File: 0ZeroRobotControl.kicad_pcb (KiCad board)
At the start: 4 copper layers, 100 x 100 mm, 249 parts, among them IC1 TC4427A, IC10 L6470, IC2 TC4427A, IC3 TC4427A, IC4 CY25811, IC5 L6470, IC6 L6470, IC7 L6470, IC8 L6470, IC9 L6470, J1 CONN_02X08, J2 CONN_02X03, J3 USB Micro-B Power Out, P1 RaspPi 40pin Conn, P10 5452027, P11 Thermistor_Inputs, P12 MOTOR-1, P13 MOTOR-2, P14 MOTOR-3, P15 MOTOR-4, P16 MOTOR-5, P17 MOTOR-6, P18 SW1, P19 SW2, P2 XT60PW-M, P20 SW3, P21 SW4, P22 SW5, P23 SW6, P25 CONN_01X01, P26 CONN_01X01, P3 XT60PW-M, P4 XT60PW-M, P5 XT30PW-F, P6 XT30PW-F, P7 XT30PW-F, P8 5452027, P9 5452027, Q1 AOT240L, Q2 AOT240L, Q3 AOT240L, Q4 AOT2618L, Q5 AOT2618L, Q6 AOT2618L, U1 LM78L12ACZ, U2 LM78L12ACZ, U3 LM78L12ACZ, U4 MCP3204, U7 R-78E3.3-1.0, U8 R-78E5.0-1.0, Y1 Crystal 32MHz

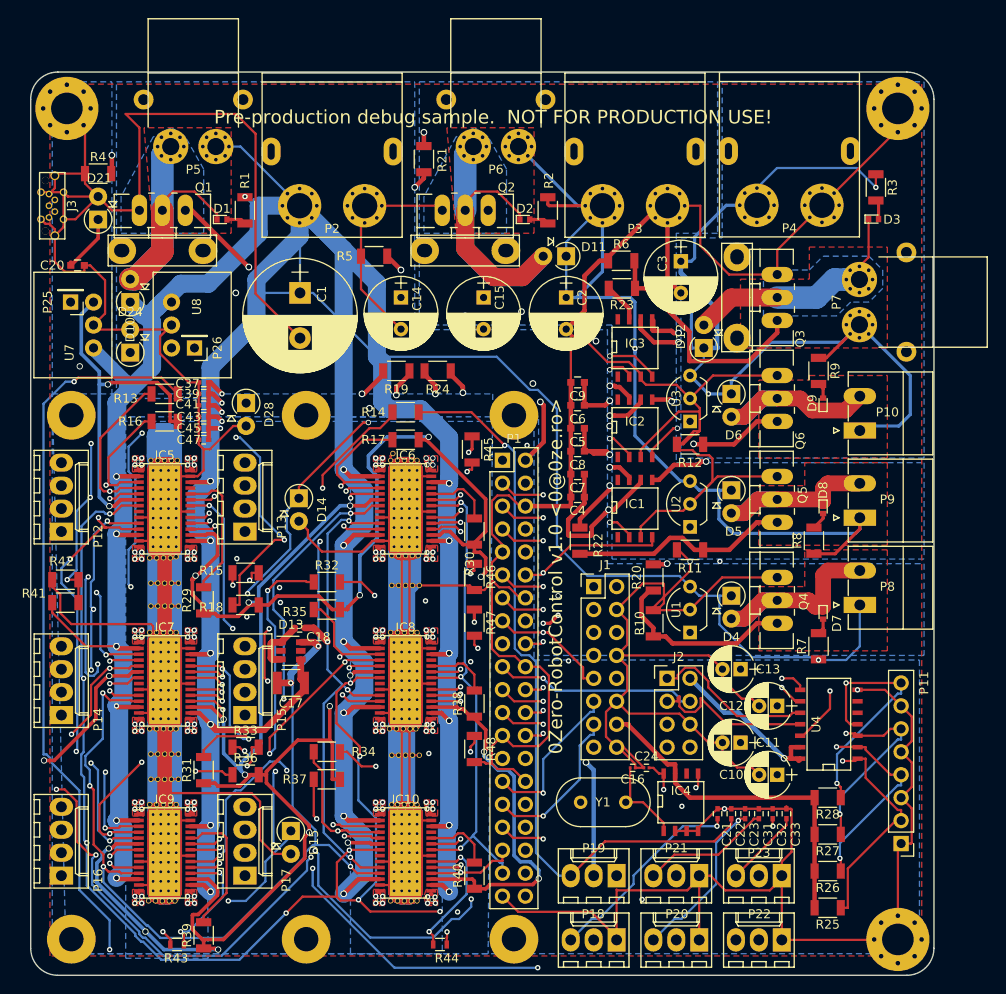
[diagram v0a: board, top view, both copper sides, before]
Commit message: added more vias for heat dispersion of stepper controllers, also fixed some tracks/vias.
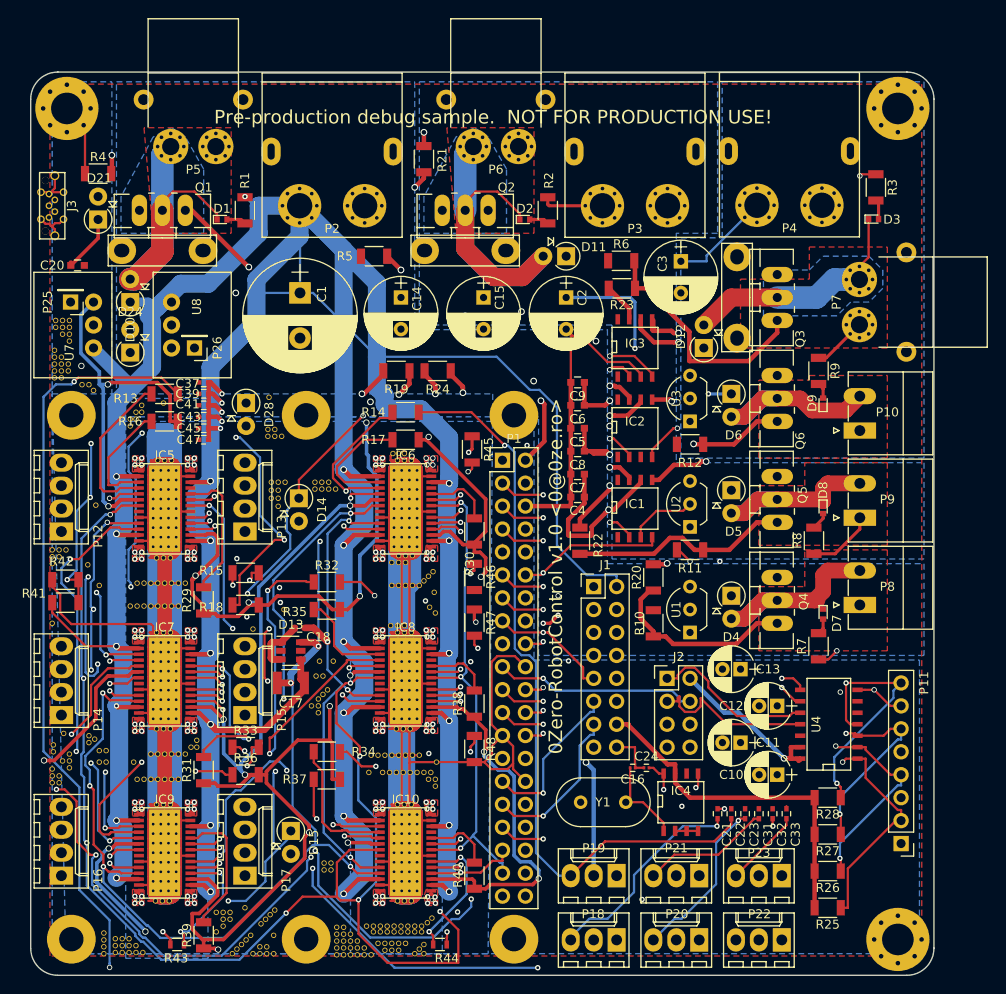
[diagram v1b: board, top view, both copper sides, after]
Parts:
- removed REF1, REF10, REF21, REF25, REF26, REF30, REF36, REF40, REF45, REF6, REF60, REF65, REF76, REF80, REF81, REF85, REF86, REF90: Via__0.6-0.4, PiPrinter:Via__0.6-0.4
- removed the REF5 at (35.3, 63.2)
- removed the REF56 at (61.8, 82.3)
- removed the REF61 at (61.7, 93.0)
- removed the REF66 at (64.8, 101.3)
- removed the REF66 at (62.0, 101.3)
- added REF42: Via__0.6-0.4, PiPrinter:Via__0.6-0.4, F.Cu at (63.5, 74.5)
- added REF42: Via__0.6-0.4, PiPrinter:Via__0.6-0.4, F.Cu at (62.7, 74.5)
- added REF5: Via__0.6-0.4, PiPrinter:Via__0.6-0.4, F.Cu at (26.3, 47.8)
- added REF5: Via__0.6-0.4, PiPrinter:Via__0.6-0.4, F.Cu at (26.2, 52.6)
- added REF5: Via__0.6-0.4, PiPrinter:Via__0.6-0.4, F.Cu at (26.2, 53.3)
- added REF5: Via__0.6-0.4, PiPrinter:Via__0.6-0.4, F.Cu at (25.4, 51.8)
- added REF5: Via__0.6-0.4, PiPrinter:Via__0.6-0.4, F.Cu at (25.4, 52.6)
- added REF5: Via__0.6-0.4, PiPrinter:Via__0.6-0.4, F.Cu at (25.4, 53.3)
- added REF5: Via__0.6-0.4, PiPrinter:Via__0.6-0.4, F.Cu at (25.4, 54.1)
- added REF5: Via__0.6-0.4, PiPrinter:Via__0.6-0.4, F.Cu at (24.6, 51.1)
- added REF5: Via__0.6-0.4, PiPrinter:Via__0.6-0.4, F.Cu at (24.6, 51.8)
- added REF5: Via__0.6-0.4, PiPrinter:Via__0.6-0.4, F.Cu at (24.6, 52.6)
- added REF5: Via__0.6-0.4, PiPrinter:Via__0.6-0.4, F.Cu at (24.6, 53.3)
- added REF5: Via__0.6-0.4, PiPrinter:Via__0.6-0.4, F.Cu at (26.3, 48.5)
- added REF5: Via__0.6-0.4, PiPrinter:Via__0.6-0.4, F.Cu at (24.6, 54.1)
- added REF5: Via__0.6-0.4, PiPrinter:Via__0.6-0.4, F.Cu at (29.0, 55.5)
- added REF5: Via__0.6-0.4, PiPrinter:Via__0.6-0.4, F.Cu at (28.4, 54.9)
- added REF5: Via__0.6-0.4, PiPrinter:Via__0.6-0.4, F.Cu at (27.7, 54.9)
- added REF5: Via__0.6-0.4, PiPrinter:Via__0.6-0.4, F.Cu at (36.7, 56.9)
- added REF5: Via__0.6-0.4, PiPrinter:Via__0.6-0.4, F.Cu at (33.0, 59.4)
- added REF5: Via__0.6-0.4, PiPrinter:Via__0.6-0.4, F.Cu at (33.0, 58.7)
- added REF5: Via__0.6-0.4, PiPrinter:Via__0.6-0.4, F.Cu at (33.7, 58.7)
- added REF5: Via__0.6-0.4, PiPrinter:Via__0.6-0.4, F.Cu at (33.7, 57.9)
- added REF5: Via__0.6-0.4, PiPrinter:Via__0.6-0.4, F.Cu at (34.3, 57.9)
- added REF5: Via__0.6-0.4, PiPrinter:Via__0.6-0.4, F.Cu at (26.3, 50.0)
- added REF5: Via__0.6-0.4, PiPrinter:Via__0.6-0.4, F.Cu at (34.3, 57.1)
- added REF5: Via__0.6-0.4, PiPrinter:Via__0.6-0.4, F.Cu at (26.3, 49.3)
- added REF5: Via__0.6-0.4, PiPrinter:Via__0.6-0.4, F.Cu at (25.5, 49.3)
- added REF5: Via__0.6-0.4, PiPrinter:Via__0.6-0.4, F.Cu at (25.5, 48.5)
- added REF5: Via__0.6-0.4, PiPrinter:Via__0.6-0.4, F.Cu at (25.5, 47.8)
- added REF5: Via__0.6-0.4, PiPrinter:Via__0.6-0.4, F.Cu at (24.8, 48.5)
- added REF5: Via__0.6-0.4, PiPrinter:Via__0.6-0.4, F.Cu at (24.8, 47.8)
- added REF50: Via__0.6-0.4, PiPrinter:Via__0.6-0.4, F.Cu at (66.8, 80.1)
- added REF50: Via__0.6-0.4, PiPrinter:Via__0.6-0.4, F.Cu at (66.2, 79.5)
- added REF50: Via__0.6-0.4, PiPrinter:Via__0.6-0.4, F.Cu at (66.5, 75.6)
- added REF50: Via__0.6-0.4, PiPrinter:Via__0.6-0.4, F.Cu at (66.0, 76.1)
- added REF50: Via__0.6-0.4, PiPrinter:Via__0.6-0.4, F.Cu at (65.5, 76.6)
- added REF56: Via__0.6-0.4, PiPrinter:Via__0.6-0.4, F.Cu at (66.7, 77.9)
- added REF56: Via__0.6-0.4, PiPrinter:Via__0.6-0.4, F.Cu at (63.4, 81.5)
- added REF56: Via__0.6-0.4, PiPrinter:Via__0.6-0.4, F.Cu at (62.6, 81.5)
- added REF56: Via__0.6-0.4, PiPrinter:Via__0.6-0.4, F.Cu at (61.8, 81.5)
- added REF61: Via__0.6-0.4, PiPrinter:Via__0.6-0.4, F.Cu at (48.4, 56.3)
- added REF61: Via__0.6-0.4, PiPrinter:Via__0.6-0.4, F.Cu at (49.4, 66.5)
- added REF61: Via__0.6-0.4, PiPrinter:Via__0.6-0.4, F.Cu at (48.6, 66.5)
- added REF61: Via__0.6-0.4, PiPrinter:Via__0.6-0.4, F.Cu at (50.2, 65.7)
- added REF61: Via__0.6-0.4, PiPrinter:Via__0.6-0.4, F.Cu at (49.4, 65.7)
- added REF61: Via__0.6-0.4, PiPrinter:Via__0.6-0.4, F.Cu at (48.6, 65.7)
- added REF61: Via__0.6-0.4, PiPrinter:Via__0.6-0.4, F.Cu at (55.8, 66.4)
- added REF61: Via__0.6-0.4, PiPrinter:Via__0.6-0.4, F.Cu at (55.0, 66.4)
- added REF61: Via__0.6-0.4, PiPrinter:Via__0.6-0.4, F.Cu at (54.2, 66.4)
- added REF61: Via__0.6-0.4, PiPrinter:Via__0.6-0.4, F.Cu at (53.5, 66.4)
- added REF61: Via__0.6-0.4, PiPrinter:Via__0.6-0.4, F.Cu at (55.0, 65.7)
- added REF61: Via__0.6-0.4, PiPrinter:Via__0.6-0.4, F.Cu at (49.8, 60.6)
- added REF61: Via__0.6-0.4, PiPrinter:Via__0.6-0.4, F.Cu at (54.2, 65.7)
- added REF61: Via__0.6-0.4, PiPrinter:Via__0.6-0.4, F.Cu at (53.5, 65.7)
- added REF61: Via__0.6-0.4, PiPrinter:Via__0.6-0.4, F.Cu at (46.6, 81.9)
- added REF61: Via__0.6-0.4, PiPrinter:Via__0.6-0.4, F.Cu at (50.0, 79.8)
- added REF61: Via__0.6-0.4, PiPrinter:Via__0.6-0.4, F.Cu at (55.5, 85.5)
- added REF61: Via__0.6-0.4, PiPrinter:Via__0.6-0.4, F.Cu at (54.0, 85.5)
- added REF61: Via__0.6-0.4, PiPrinter:Via__0.6-0.4, F.Cu at (54.4, 87.1)
- added REF61: Via__0.6-0.4, PiPrinter:Via__0.6-0.4, F.Cu at (53.6, 87.1)
- added REF61: Via__0.6-0.4, PiPrinter:Via__0.6-0.4, F.Cu at (53.1, 90.4)
- added REF61: Via__0.6-0.4, PiPrinter:Via__0.6-0.4, F.Cu at (53.8, 91.2)
- added REF61: Via__0.6-0.4, PiPrinter:Via__0.6-0.4, F.Cu at (49.0, 60.6)
- added REF61: Via__0.6-0.4, PiPrinter:Via__0.6-0.4, F.Cu at (53.8, 90.4)
- added REF61: Via__0.6-0.4, PiPrinter:Via__0.6-0.4, F.Cu at (53.8, 89.7)
- added REF61: Via__0.6-0.4, PiPrinter:Via__0.6-0.4, F.Cu at (54.4, 89.2)
- added REF61: Via__0.6-0.4, PiPrinter:Via__0.6-0.4, F.Cu at (54.9, 88.6)
- added REF61: Via__0.6-0.4, PiPrinter:Via__0.6-0.4, F.Cu at (48.3, 60.6)
- added REF61: Via__0.6-0.4, PiPrinter:Via__0.6-0.4, F.Cu at (49.0, 59.8)
- added REF61: Via__0.6-0.4, PiPrinter:Via__0.6-0.4, F.Cu at (48.3, 59.8)
- added REF61: Via__0.6-0.4, PiPrinter:Via__0.6-0.4, F.Cu at (49.4, 68.3)
- added REF61: Via__0.6-0.4, PiPrinter:Via__0.6-0.4, F.Cu at (49.4, 67.4)
- added REF61: Via__0.6-0.4, PiPrinter:Via__0.6-0.4, F.Cu at (48.6, 67.4)
- added REF70: Via__0.6-0.4, PiPrinter:Via__0.6-0.4, F.Cu at (25.1, 98.2)
- added REF70: Via__0.6-0.4, PiPrinter:Via__0.6-0.4, F.Cu at (25.1, 73.2)
- added REF70: Via__0.6-0.4, PiPrinter:Via__0.6-0.4, F.Cu at (55.9, 117.2)
- added REF70: Via__0.6-0.4, PiPrinter:Via__0.6-0.4, F.Cu at (58.2, 116.5)
- added REF70: Via__0.6-0.4, PiPrinter:Via__0.6-0.4, F.Cu at (57.4, 116.5)
- added REF70: Via__0.6-0.4, PiPrinter:Via__0.6-0.4, F.Cu at (56.6, 116.5)
- added REF70: Via__0.6-0.4, PiPrinter:Via__0.6-0.4, F.Cu at (55.9, 116.5)
- added REF70: Via__0.6-0.4, PiPrinter:Via__0.6-0.4, F.Cu at (57.4, 115.7)
- added REF70: Via__0.6-0.4, PiPrinter:Via__0.6-0.4, F.Cu at (56.6, 115.7)
- added REF70: Via__0.6-0.4, PiPrinter:Via__0.6-0.4, F.Cu at (55.9, 115.7)
- added REF70: Via__0.6-0.4, PiPrinter:Via__0.6-0.4, F.Cu at (56.6, 114.9)
- added REF70: Via__0.6-0.4, PiPrinter:Via__0.6-0.4, F.Cu at (55.9, 114.9)
- added REF70: Via__0.6-0.4, PiPrinter:Via__0.6-0.4, F.Cu at (24.4, 74.7)
- added REF70: Via__0.6-0.4, PiPrinter:Via__0.6-0.4, F.Cu at (65.5, 117.9)
- added REF70: Via__0.6-0.4, PiPrinter:Via__0.6-0.4, F.Cu at (64.5, 117.9)
- added REF70: Via__0.6-0.4, PiPrinter:Via__0.6-0.4, F.Cu at (65.0, 117.3)
- added REF70: Via__0.6-0.4, PiPrinter:Via__0.6-0.4, F.Cu at (65.5, 116.8)
- added REF70: Via__0.6-0.4, PiPrinter:Via__0.6-0.4, F.Cu at (62.7, 117.5)
- added REF70: Via__0.6-0.4, PiPrinter:Via__0.6-0.4, F.Cu at (62.0, 117.5)
- added REF70: Via__0.6-0.4, PiPrinter:Via__0.6-0.4, F.Cu at (61.2, 117.5)
- added REF70: Via__0.6-0.4, PiPrinter:Via__0.6-0.4, F.Cu at (63.5, 116.7)
- added REF70: Via__0.6-0.4, PiPrinter:Via__0.6-0.4, F.Cu at (62.7, 116.7)
- added REF70: Via__0.6-0.4, PiPrinter:Via__0.6-0.4, F.Cu at (62.0, 116.7)
- added REF70: Via__0.6-0.4, PiPrinter:Via__0.6-0.4, F.Cu at (24.4, 73.9)
- added REF70: Via__0.6-0.4, PiPrinter:Via__0.6-0.4, F.Cu at (61.2, 116.7)
- added REF70: Via__0.6-0.4, PiPrinter:Via__0.6-0.4, F.Cu at (60.5, 116.7)
- added REF70: Via__0.6-0.4, PiPrinter:Via__0.6-0.4, F.Cu at (65.3, 115.4)
- added REF70: Via__0.6-0.4, PiPrinter:Via__0.6-0.4, F.Cu at (64.5, 115.4)
- added REF70: Via__0.6-0.4, PiPrinter:Via__0.6-0.4, F.Cu at (63.8, 115.4)
- added REF70: Via__0.6-0.4, PiPrinter:Via__0.6-0.4, F.Cu at (63.0, 115.4)
- added REF70: Via__0.6-0.4, PiPrinter:Via__0.6-0.4, F.Cu at (62.2, 115.4)
- added REF70: Via__0.6-0.4, PiPrinter:Via__0.6-0.4, F.Cu at (61.5, 115.4)
- added REF70: Via__0.6-0.4, PiPrinter:Via__0.6-0.4, F.Cu at (60.7, 115.4)
- added REF70: Via__0.6-0.4, PiPrinter:Via__0.6-0.4, F.Cu at (59.9, 115.4)
- added REF70: Via__0.6-0.4, PiPrinter:Via__0.6-0.4, F.Cu at (24.4, 73.2)
- added REF70: Via__0.6-0.4, PiPrinter:Via__0.6-0.4, F.Cu at (66.4, 113.9)
- added REF70: Via__0.6-0.4, PiPrinter:Via__0.6-0.4, F.Cu at (65.9, 114.4)
- added REF70: Via__0.6-0.4, PiPrinter:Via__0.6-0.4, F.Cu at (65.3, 114.8)
- added REF70: Via__0.6-0.4, PiPrinter:Via__0.6-0.4, F.Cu at (64.5, 114.8)
- added REF70: Via__0.6-0.4, PiPrinter:Via__0.6-0.4, F.Cu at (63.8, 114.8)
- added REF70: Via__0.6-0.4, PiPrinter:Via__0.6-0.4, F.Cu at (63.0, 114.8)
- added REF70: Via__0.6-0.4, PiPrinter:Via__0.6-0.4, F.Cu at (62.2, 114.8)
- added REF70: Via__0.6-0.4, PiPrinter:Via__0.6-0.4, F.Cu at (61.5, 114.8)
- added REF70: Via__0.6-0.4, PiPrinter:Via__0.6-0.4, F.Cu at (60.7, 114.8)
- added REF70: Via__0.6-0.4, PiPrinter:Via__0.6-0.4, F.Cu at (59.9, 114.8)
- added REF70: Via__0.6-0.4, PiPrinter:Via__0.6-0.4, F.Cu at (24.4, 81.3)
- added REF70: Via__0.6-0.4, PiPrinter:Via__0.6-0.4, F.Cu at (59.2, 114.8)
- added REF70: Via__0.6-0.4, PiPrinter:Via__0.6-0.4, F.Cu at (66.9, 96.6)
- added REF70: Via__0.6-0.4, PiPrinter:Via__0.6-0.4, F.Cu at (61.0, 97.8)
- added REF70: Via__0.6-0.4, PiPrinter:Via__0.6-0.4, F.Cu at (61.7, 97.8)
- added REF70: Via__0.6-0.4, PiPrinter:Via__0.6-0.4, F.Cu at (62.5, 97.8)
- added REF70: Via__0.6-0.4, PiPrinter:Via__0.6-0.4, F.Cu at (59.7, 95.9)
- added REF70: Via__0.6-0.4, PiPrinter:Via__0.6-0.4, F.Cu at (60.5, 95.9)
- added REF70: Via__0.6-0.4, PiPrinter:Via__0.6-0.4, F.Cu at (61.2, 95.9)
- added REF70: Via__0.6-0.4, PiPrinter:Via__0.6-0.4, F.Cu at (66.8, 99.3)
- added REF70: Via__0.6-0.4, PiPrinter:Via__0.6-0.4, F.Cu at (66.8, 98.6)
- added REF70: Via__0.6-0.4, PiPrinter:Via__0.6-0.4, F.Cu at (28.3, 74.8)
- added REF70: Via__0.6-0.4, PiPrinter:Via__0.6-0.4, F.Cu at (66.0, 98.6)
- added REF70: Via__0.6-0.4, PiPrinter:Via__0.6-0.4, F.Cu at (66.3, 97.8)
- added REF70: Via__0.6-0.4, PiPrinter:Via__0.6-0.4, F.Cu at (65.5, 97.8)
- added REF70: Via__0.6-0.4, PiPrinter:Via__0.6-0.4, F.Cu at (64.8, 97.8)
- added REF70: Via__0.6-0.4, PiPrinter:Via__0.6-0.4, F.Cu at (29.6, 77.1)
- added REF70: Via__0.6-0.4, PiPrinter:Via__0.6-0.4, F.Cu at (39.1, 76.8)
- added REF70: Via__0.6-0.4, PiPrinter:Via__0.6-0.4, F.Cu at (33.8, 76.8)
- added REF70: Via__0.6-0.4, PiPrinter:Via__0.6-0.4, F.Cu at (34.5, 76.8)
- added REF70: Via__0.6-0.4, PiPrinter:Via__0.6-0.4, F.Cu at (30.1, 117.9)
- added REF70: Via__0.6-0.4, PiPrinter:Via__0.6-0.4, F.Cu at (33.0, 79.4)
- added REF70: Via__0.6-0.4, PiPrinter:Via__0.6-0.4, F.Cu at (33.8, 79.4)
- added REF70: Via__0.6-0.4, PiPrinter:Via__0.6-0.4, F.Cu at (34.5, 79.4)
- added REF70: Via__0.6-0.4, PiPrinter:Via__0.6-0.4, F.Cu at (24.4, 98.9)
- added REF70: Via__0.6-0.4, PiPrinter:Via__0.6-0.4, F.Cu at (24.4, 98.2)
- added REF70: Via__0.6-0.4, PiPrinter:Via__0.6-0.4, F.Cu at (24.4, 97.4)
- added REF70: Via__0.6-0.4, PiPrinter:Via__0.6-0.4, F.Cu at (25.1, 98.9)
- added REF70: Via__0.6-0.4, PiPrinter:Via__0.6-0.4, F.Cu at (25.7, 93.5)
- added REF70: Via__0.6-0.4, PiPrinter:Via__0.6-0.4, F.Cu at (24.5, 94.7)
- added REF70: Via__0.6-0.4, PiPrinter:Via__0.6-0.4, F.Cu at (24.5, 95.5)
- added REF70: Via__0.6-0.4, PiPrinter:Via__0.6-0.4, F.Cu at (31.4, 117.7)
- added REF70: Via__0.6-0.4, PiPrinter:Via__0.6-0.4, F.Cu at (26.3, 97.3)
- added REF70: Via__0.6-0.4, PiPrinter:Via__0.6-0.4, F.Cu at (26.3, 95.8)
- added REF70: Via__0.6-0.4, PiPrinter:Via__0.6-0.4, F.Cu at (26.3, 96.5)
- added REF70: Via__0.6-0.4, PiPrinter:Via__0.6-0.4, F.Cu at (25.5, 96.5)
- added REF70: Via__0.6-0.4, PiPrinter:Via__0.6-0.4, F.Cu at (29.1, 94.1)
- added REF70: Via__0.6-0.4, PiPrinter:Via__0.6-0.4, F.Cu at (28.4, 94.5)
- added REF70: Via__0.6-0.4, PiPrinter:Via__0.6-0.4, F.Cu at (28.4, 93.7)
- added REF70: Via__0.6-0.4, PiPrinter:Via__0.6-0.4, F.Cu at (29.6, 95.4)
- added REF70: Via__0.6-0.4, PiPrinter:Via__0.6-0.4, F.Cu at (30.4, 95.4)
- added REF70: Via__0.6-0.4, PiPrinter:Via__0.6-0.4, F.Cu at (29.6, 96.6)
- added REF70: Via__0.6-0.4, PiPrinter:Via__0.6-0.4, F.Cu at (59.4, 97.8)
- added REF70: Via__0.6-0.4, PiPrinter:Via__0.6-0.4, F.Cu at (30.4, 96.6)
- added REF70: Via__0.6-0.4, PiPrinter:Via__0.6-0.4, F.Cu at (40.4, 94.2)
- added REF70: Via__0.6-0.4, PiPrinter:Via__0.6-0.4, F.Cu at (40.4, 95.0)
- added REF70: Via__0.6-0.4, PiPrinter:Via__0.6-0.4, F.Cu at (39.8, 95.0)
- added REF70: Via__0.6-0.4, PiPrinter:Via__0.6-0.4, F.Cu at (39.1, 95.8)
- added REF70: Via__0.6-0.4, PiPrinter:Via__0.6-0.4, F.Cu at (33.4, 96.6)
- added REF70: Via__0.6-0.4, PiPrinter:Via__0.6-0.4, F.Cu at (33.8, 98.6)
- added REF70: Via__0.6-0.4, PiPrinter:Via__0.6-0.4, F.Cu at (34.5, 98.6)
- added REF70: Via__0.6-0.4, PiPrinter:Via__0.6-0.4, F.Cu at (42.5, 115.4)
- added REF70: Via__0.6-0.4, PiPrinter:Via__0.6-0.4, F.Cu at (43.3, 114.8)
- added REF70: Via__0.6-0.4, PiPrinter:Via__0.6-0.4, F.Cu at (64.0, 97.8)
- added REF70: Via__0.6-0.4, PiPrinter:Via__0.6-0.4, F.Cu at (44.1, 114.0)
- added REF70: Via__0.6-0.4, PiPrinter:Via__0.6-0.4, F.Cu at (43.3, 114.0)
- added REF70: Via__0.6-0.4, PiPrinter:Via__0.6-0.4, F.Cu at (44.1, 113.3)
- added REF70: Via__0.6-0.4, PiPrinter:Via__0.6-0.4, F.Cu at (42.5, 113.3)
- added REF70: Via__0.6-0.4, PiPrinter:Via__0.6-0.4, F.Cu at (43.3, 113.3)
- added REF70: Via__0.6-0.4, PiPrinter:Via__0.6-0.4, F.Cu at (45.7, 112.8)
- added REF70: Via__0.6-0.4, PiPrinter:Via__0.6-0.4, F.Cu at (49.0, 113.0)
- added REF70: Via__0.6-0.4, PiPrinter:Via__0.6-0.4, F.Cu at (48.5, 113.5)
- added REF70: Via__0.6-0.4, PiPrinter:Via__0.6-0.4, F.Cu at (48.0, 114.0)
- added REF70: Via__0.6-0.4, PiPrinter:Via__0.6-0.4, F.Cu at (47.5, 114.6)
- added REF70: Via__0.6-0.4, PiPrinter:Via__0.6-0.4, F.Cu at (63.2, 97.8)
- added REF70: Via__0.6-0.4, PiPrinter:Via__0.6-0.4, F.Cu at (46.4, 115.8)
- added REF70: Via__0.6-0.4, PiPrinter:Via__0.6-0.4, F.Cu at (45.8, 116.3)
- added REF70: Via__0.6-0.4, PiPrinter:Via__0.6-0.4, F.Cu at (45.3, 116.8)
- added REF70: Via__0.6-0.4, PiPrinter:Via__0.6-0.4, F.Cu at (44.8, 117.3)
- added REF70: Via__0.6-0.4, PiPrinter:Via__0.6-0.4, F.Cu at (44.3, 117.9)
- added REF70: Via__0.6-0.4, PiPrinter:Via__0.6-0.4, F.Cu at (30.1, 117.1)
- added REF70: Via__0.6-0.4, PiPrinter:Via__0.6-0.4, F.Cu at (30.1, 115.6)
- added REF70: Via__0.6-0.4, PiPrinter:Via__0.6-0.4, F.Cu at (30.1, 116.3)
- added REF70: Via__0.6-0.4, PiPrinter:Via__0.6-0.4, F.Cu at (34.4, 117.7)
- added REF70: Via__0.6-0.4, PiPrinter:Via__0.6-0.4, F.Cu at (33.7, 117.7)
- added REF70: Via__0.6-0.4, PiPrinter:Via__0.6-0.4, F.Cu at (29.2, 68.2)
- added REF70: Via__0.6-0.4, PiPrinter:Via__0.6-0.4, F.Cu at (32.9, 117.7)
- added REF70: Via__0.6-0.4, PiPrinter:Via__0.6-0.4, F.Cu at (32.1, 117.7)
- added REF70: Via__0.6-0.4, PiPrinter:Via__0.6-0.4, F.Cu at (33.7, 117.0)
- added REF70: Via__0.6-0.4, PiPrinter:Via__0.6-0.4, F.Cu at (32.9, 117.0)
- added REF70: Via__0.6-0.4, PiPrinter:Via__0.6-0.4, F.Cu at (32.1, 117.0)
- added REF70: Via__0.6-0.4, PiPrinter:Via__0.6-0.4, F.Cu at (31.4, 117.0)
- added REF70: Via__0.6-0.4, PiPrinter:Via__0.6-0.4, F.Cu at (32.9, 116.2)
- added REF70: Via__0.6-0.4, PiPrinter:Via__0.6-0.4, F.Cu at (32.1, 116.2)
- added REF70: Via__0.6-0.4, PiPrinter:Via__0.6-0.4, F.Cu at (31.4, 116.2)
- added REF70: Via__0.6-0.4, PiPrinter:Via__0.6-0.4, F.Cu at (48.9, 115.8)
- added REF70: Via__0.6-0.4, PiPrinter:Via__0.6-0.4, F.Cu at (25.1, 73.9)
- added REF70: Via__0.6-0.4, PiPrinter:Via__0.6-0.4, F.Cu at (48.1, 117.1)
- added REF70: Via__0.6-0.4, PiPrinter:Via__0.6-0.4, F.Cu at (47.4, 117.1)
- added REF70: Via__0.6-0.4, PiPrinter:Via__0.6-0.4, F.Cu at (48.9, 117.9)
- added REF70: Via__0.6-0.4, PiPrinter:Via__0.6-0.4, F.Cu at (48.1, 117.9)
- added REF70: Via__0.6-0.4, PiPrinter:Via__0.6-0.4, F.Cu at (47.4, 117.9)
- added REF70: Via__0.6-0.4, PiPrinter:Via__0.6-0.4, F.Cu at (46.6, 117.9)
- added REF70: Via__0.6-0.4, PiPrinter:Via__0.6-0.4, F.Cu at (54.5, 108.6)
- added REF70: Via__0.6-0.4, PiPrinter:Via__0.6-0.4, F.Cu at (55.2, 108.6)
- added REF70: Via__0.6-0.4, PiPrinter:Via__0.6-0.4, F.Cu at (55.2, 107.8)
- added REF70: Via__0.6-0.4, PiPrinter:Via__0.6-0.4, F.Cu at (54.5, 107.8)
- added REF70: Via__0.6-0.4, PiPrinter:Via__0.6-0.4, F.Cu at (25.9, 73.2)
- added REF70: Via__0.6-0.4, PiPrinter:Via__0.6-0.4, F.Cu at (59.7, 118.0)
- added REF70: Via__0.6-0.4, PiPrinter:Via__0.6-0.4, F.Cu at (58.9, 118.0)
- added REF70: Via__0.6-0.4, PiPrinter:Via__0.6-0.4, F.Cu at (58.2, 118.0)
- added REF70: Via__0.6-0.4, PiPrinter:Via__0.6-0.4, F.Cu at (57.4, 118.0)
- added REF70: Via__0.6-0.4, PiPrinter:Via__0.6-0.4, F.Cu at (56.6, 118.0)
- added REF70: Via__0.6-0.4, PiPrinter:Via__0.6-0.4, F.Cu at (55.9, 118.0)
- added REF70: Via__0.6-0.4, PiPrinter:Via__0.6-0.4, F.Cu at (58.9, 117.2)
- added REF70: Via__0.6-0.4, PiPrinter:Via__0.6-0.4, F.Cu at (58.2, 117.2)
- added REF70: Via__0.6-0.4, PiPrinter:Via__0.6-0.4, F.Cu at (57.4, 117.2)
- added REF70: Via__0.6-0.4, PiPrinter:Via__0.6-0.4, F.Cu at (56.6, 117.2)
- added REF96: Via__0.6-0.4, PiPrinter:Via__0.6-0.4, F.Cu at (63.4, 62.5)
- added REF96: Via__0.6-0.4, PiPrinter:Via__0.6-0.4, F.Cu at (62.7, 62.5)
- moved REF41 0.76 mm to (62.0, 74.5)
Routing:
- net GND: track 1778.9 -> 1241.5 mm
- net /VBB3: track 157.5 -> 80.8 mm
- net /VBB2: track 143.0 -> 71.2 mm
- net /VBB1: track 602.5 -> 558.8 mm
- net /Steppers/SSCLK: track 224.3 -> 236.4 mm, vias 15 -> 14
- net /3.3VR: track 554.1 -> 558.2 mm
- net Net-(IC6-Pad4): track 19.0 -> 16.7 mm, vias 2 -> 1
- net /SW1: track 156.7 -> 158.9 mm
- net /Steppers/CP1: track 165.4 -> 164.0 mm, vias 12 -> 11
- net /Steppers/CP0: track 164.2 -> 165.2 mm
- net /Steppers/ADC_VChk2: track 116.4 -> 117.3 mm
- net /5VR: track 185.3 -> 184.4 mm
- net Net-(IC6-Pad3): track 13.9 -> 13.3 mm, vias 1 -> 0
- net Net-(IC8-Pad3): track 11.3 -> 10.9 mm, vias 1 -> 0
- net Net-(IC5-Pad3): track 13.3 -> 13.0 mm, vias 1 -> 0
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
